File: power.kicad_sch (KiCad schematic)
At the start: 14 parts, among them SW1 SW_SPDT, U1 TP4054, U2 XC6206PxxxMR

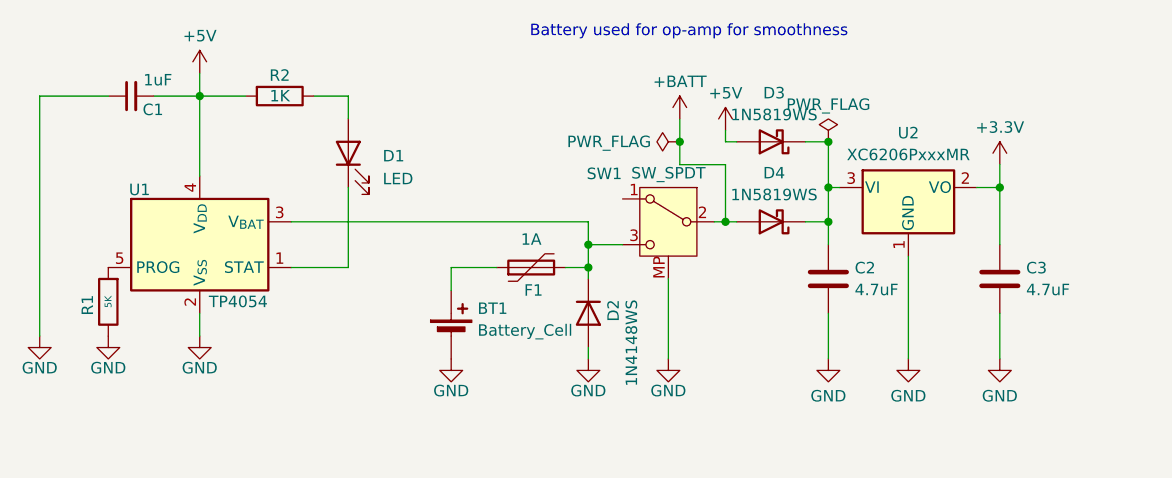
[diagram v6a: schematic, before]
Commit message: v4.1, see commit for details
Added passthrough hole for battery wires for users soldering batteries in
Cleared ground plane under screw holes
Uses only 3.5mm tip for stylus and sleeve for the pedal
Better anchoring for the 2.5mm jack for improved durability
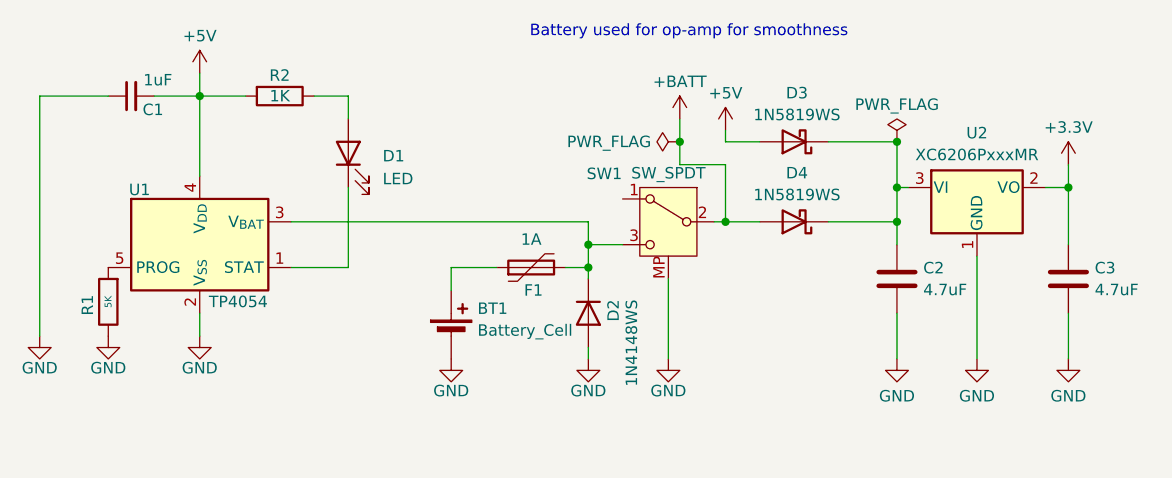
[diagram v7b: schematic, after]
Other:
- moved on the sheet: C2, C3, D3, D4, U2
